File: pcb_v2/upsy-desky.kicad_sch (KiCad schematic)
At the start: 62 parts, among them J1 RJ45, J2 RJ45, J3 USB_C_ReceptacleUSB2.0, J4 Conn_01x03_Socket, J5 Screw_Terminal_01x03, J6 Conn_01x03_Pin, Q3 2N7002, Q4 2N7002, Q5 2N7002, Q6 2N7002, Q7 2N7002, Q8 2N7002, SW1 SW_Push, U1 VL53L0CXV0DH1, U2 AMS1117-3.3, U4 ESP32-C3-WROOM-02, Y1 32K

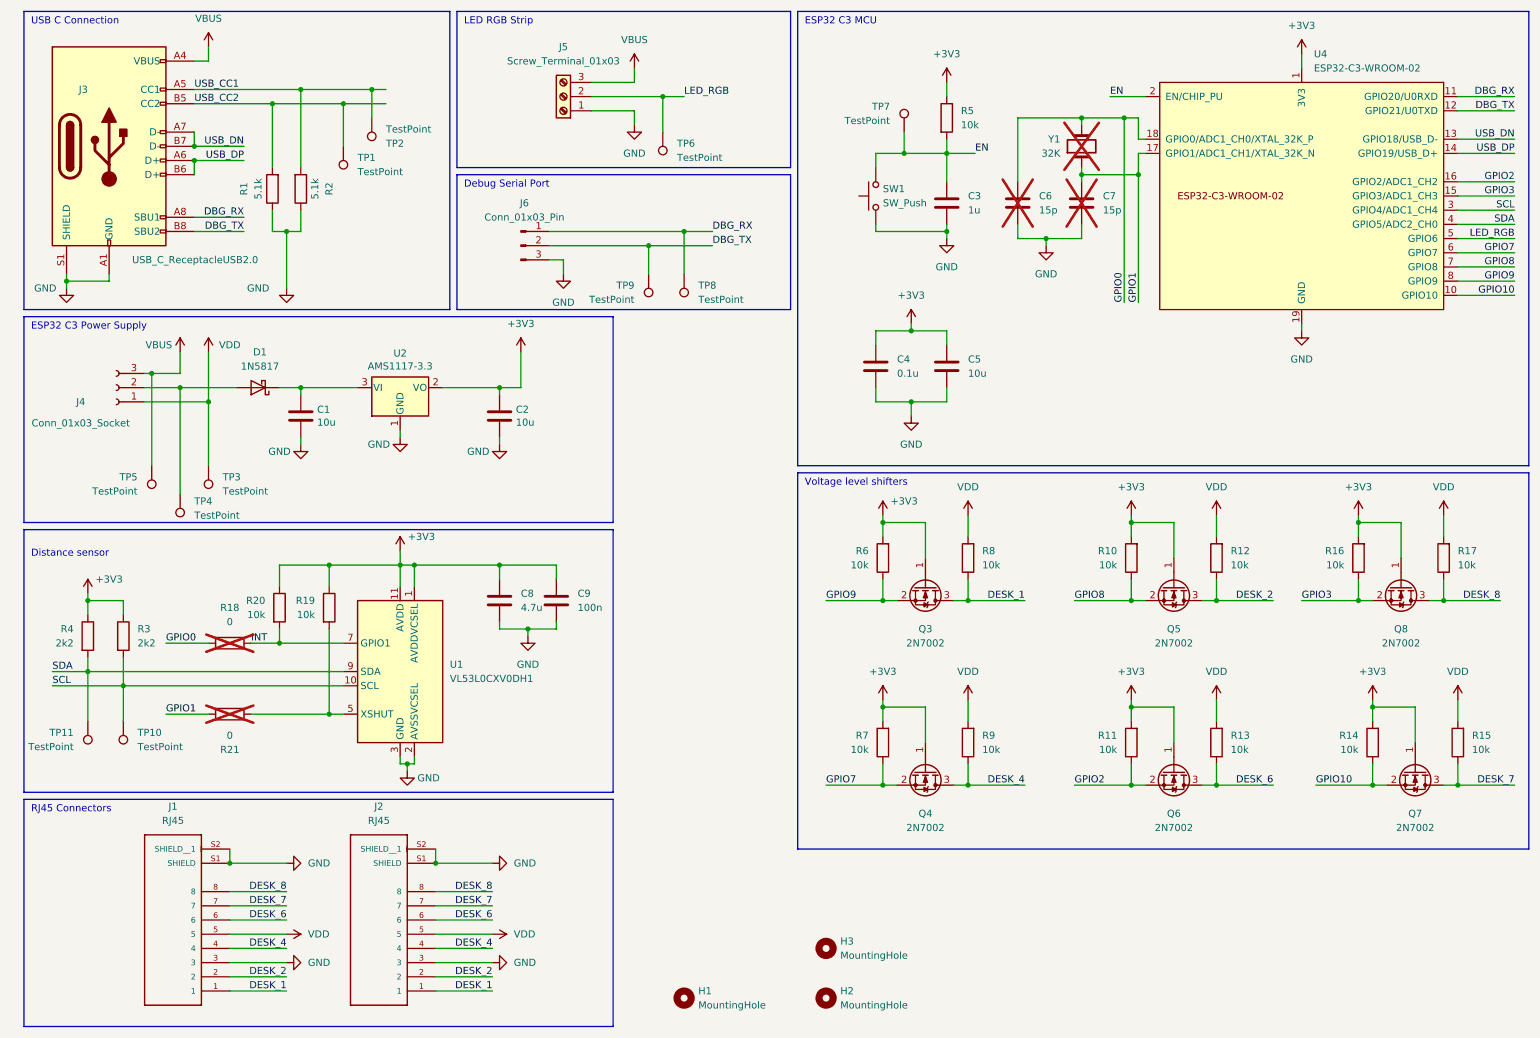
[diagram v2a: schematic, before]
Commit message: Switch to heirarchical layout - add usb, controller and connectors sheets.
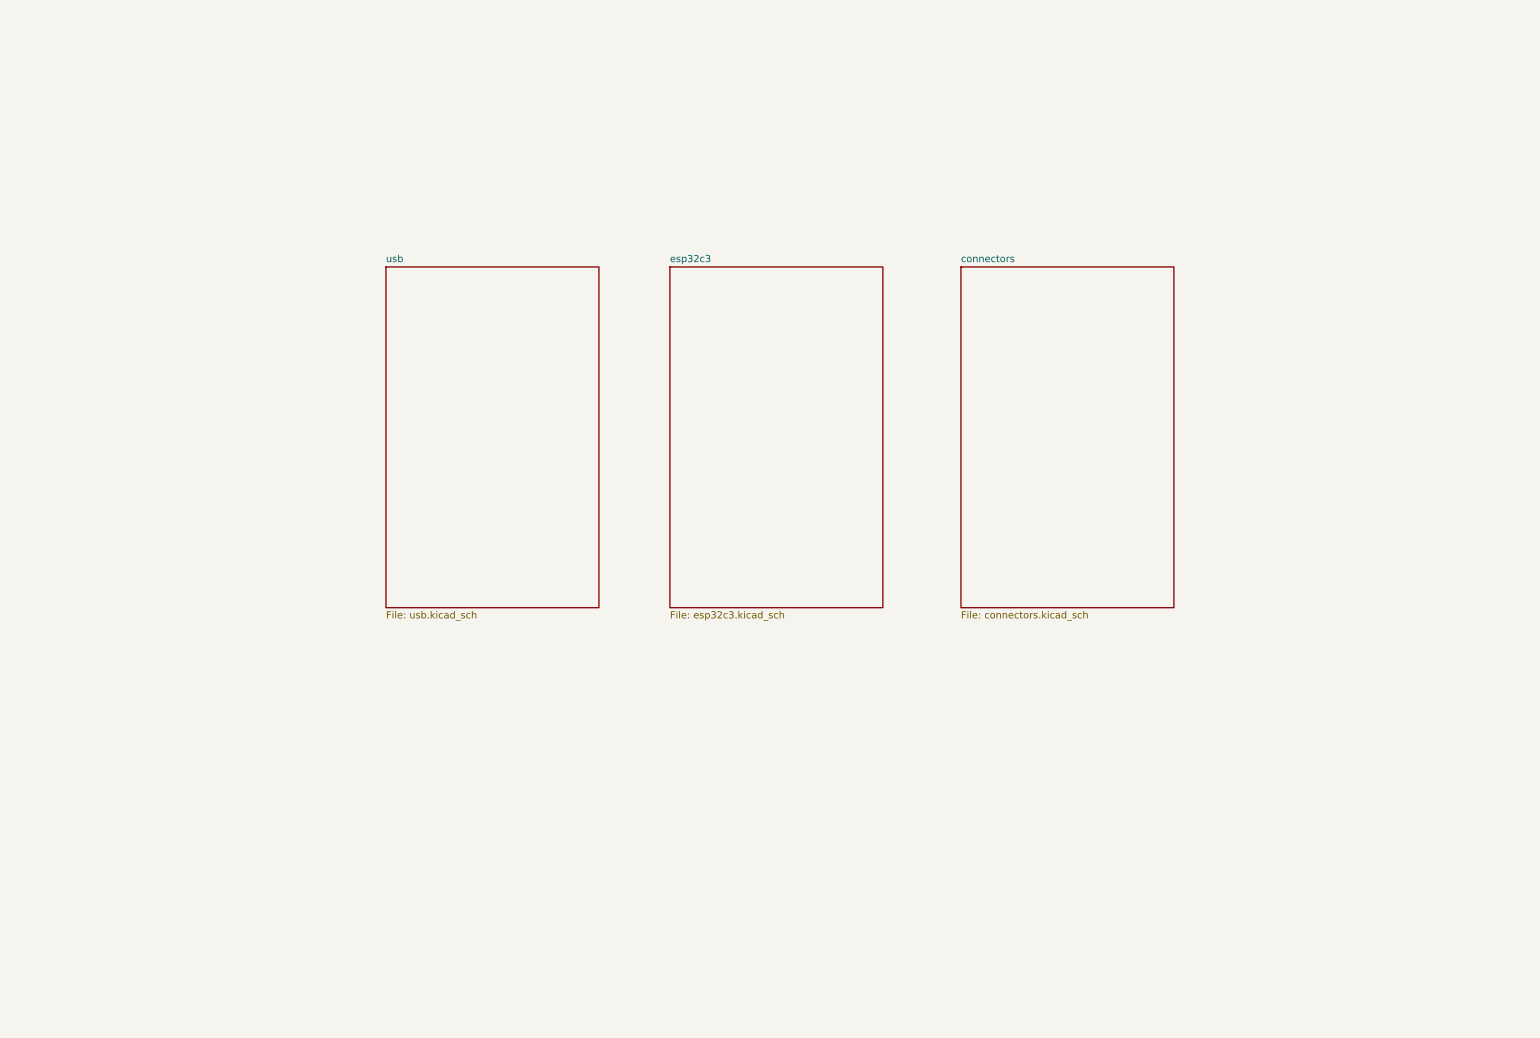
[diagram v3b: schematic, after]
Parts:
- removed C1, C2, C5: 10u, Capacitor_SMD:C_0402_1005Metric, symbol Device:C
- removed C3: 1u, Capacitor_SMD:C_0402_1005Metric, symbol Device:C
- removed C4: 0.1u, Capacitor_SMD:C_0402_1005Metric, symbol Device:C
- removed C6, C7: 15p, Capacitor_SMD:C_0402_1005Metric, symbol Device:C
- removed C8: 4.7u, Capacitor_SMD:C_0402_1005Metric, symbol Device:C
- removed C9: 100n, Capacitor_SMD:C_0402_1005Metric, symbol Device:C
- removed D1: 1N5817, Diode_SMD:D_SOD-323, symbol Diode:1N5817
- removed H1, H2, H3: MountingHole, MountingHole:MountingHole_2.2mm_M2_Pad, symbol Mechanical:MountingHole
- removed J1, J2: RJ45, Connector_RJ:RJ45_Amphenol_54602-x08_Horizontal, symbol A-2004-2-4-LPS-N-R:A-2004-2-4-LPS-N-R
- removed J3: USB_C_ReceptacleUSB2.0, Connector_USB:USB_C_Receptacle_Palconn_UTC16-G, symbol Connector:USB_C_Receptacle_USB2.0
- removed J4: Conn_01x03_Socket, Connector:FanPinHeader_1x03_P2.54mm_Vertical, symbol Connector:Conn_01x03_Socket
- removed J5: Screw_Terminal_01x03, TerminalBlock:TerminalBlock_Altech_AK300-3_P5.00mm, symbol Connector:Screw_Terminal_01x03
- removed J6: Conn_01x03_Pin, Connector_JST:JST_EH_B3B-EH-A_1x03_P2.50mm_Vertical, symbol Connector:Conn_01x03_Pin
- removed Q3, Q4, Q5, Q6, Q7, Q8: 2N7002, Package_TO_SOT_SMD:SOT-23, symbol Transistor_FET:BSS138
- removed R1, R2: 5.1k, Resistor_SMD:R_0402_1005Metric, symbol Device:R
- removed R10, R11, R12, R13, R14, R15, R16, R17, R19, R20, R5, R6, R7, R8, R9: 10k, Resistor_SMD:R_0402_1005Metric, symbol Device:R
- removed R18, R21: 0, Resistor_SMD:R_0402_1005Metric, symbol Device:R
- removed R3, R4: 2k2, Resistor_SMD:R_0402_1005Metric, symbol Device:R
- removed SW1: SW_Push, Button_Switch_SMD:SW_Push_1P1T_NO_CK_KMR2, symbol Switch:SW_Push
- removed TP1, TP10, TP11, TP2, TP3, TP4, TP5, TP6, TP7, TP8, TP9: TestPoint, TestPoint:TestPoint_Pad_D1.0mm, symbol Connector:TestPoint
- removed U1: VL53L0CXV0DH1, Sensor_Distance:ST_VL53L1x, symbol Sensor_Distance:VL53L0CXV0DH1
- removed U2: AMS1117-3.3, Package_TO_SOT_SMD:SOT-223-3_TabPin2, symbol Regulator_Linear:NCP1117-3.3_SOT223
- removed U4: ESP32-C3-WROOM-02, PCM_Espressif:ESP32-C3-WROOM-02, symbol PCM_Espressif:ESP32-C3-WROOM-02
- removed Y1: 32K, Crystal:Crystal_SMD_2012-2Pin_2.0x1.2mm, symbol Device:Crystal
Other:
- added sheet connectors (connectors.kicad_sch)
- added sheet esp32c3 (esp32c3.kicad_sch)
- added sheet usb (usb.kicad_sch)
- note removed: "Debug Serial Port"
- note removed: "Distance sensor"
- note removed: "ESP32 C3 MCU"
- note removed: "ESP32 C3 Power Supply"
- note removed: "LED RGB Strip"
- note removed: "RJ45 Connectors"
- note removed: "USB C Connection"
- note removed: "Voltage level shifters"

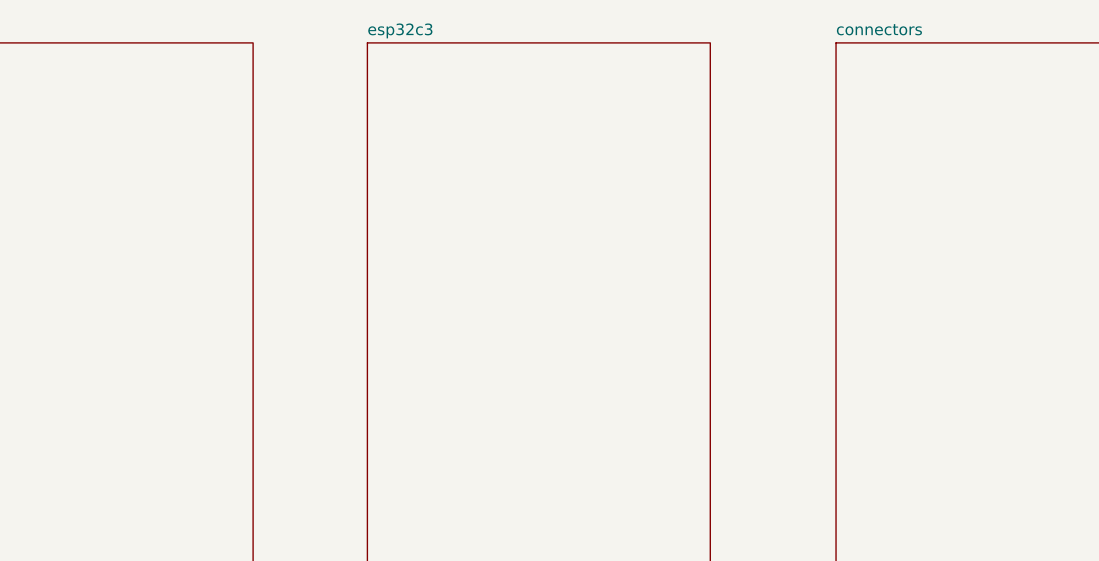
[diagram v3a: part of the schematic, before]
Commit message: Connect pin sheets. Add protection on USB. Use SolderJumpers.
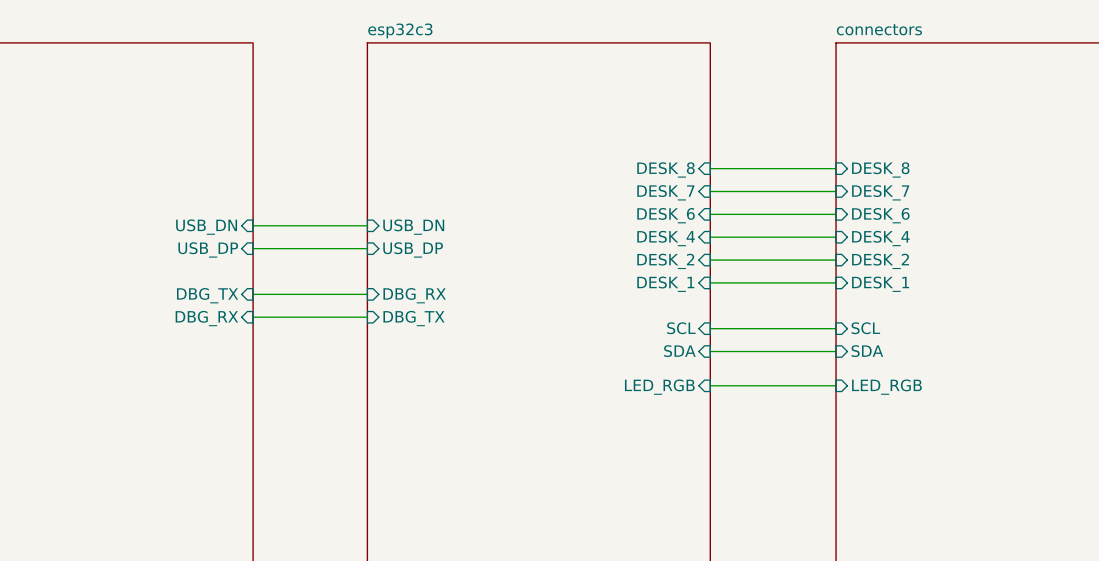
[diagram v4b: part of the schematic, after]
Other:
- sheet connectors ports: added DESK_1, DESK_2, DESK_4, DESK_6, DESK_7, DESK_8, LED_RGB, SCL, SDA; removed none
- sheet esp32c3 ports: added DBG_RX, DBG_TX, DESK_1, DESK_2, DESK_4, DESK_6, DESK_7, DESK_8, LED_RGB, SCL, SDA, USB_DN, USB_DP; removed none
- sheet usb ports: added DBG_RX, DBG_TX, USB_DN, USB_DP; removed none
